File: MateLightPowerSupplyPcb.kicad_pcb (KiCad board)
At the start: 2 copper layers, 59 x 30 mm, 22 parts, among them X1 Power IN, X10 JST ZE 2, X11 JST ZE 2, X12 JST ZE 2, X13 JST ZE 2, X14 JST ZE 2, X15 JST ZE 2, X16 JST ZE 2, X17 JST ZE 2, X18 JST ZE 2, X19 JST ZE 2, X2 Power Out, X20 JST ZE 2, X21 JST ZE 2, X22 JST ZE 2, X3 JST ZE 2, X4 JST ZE 2, X5 JST ZE 2, X6 JST ZE 2, X7 JST ZE 2, X8 JST ZE 2, X9 JST ZE 2

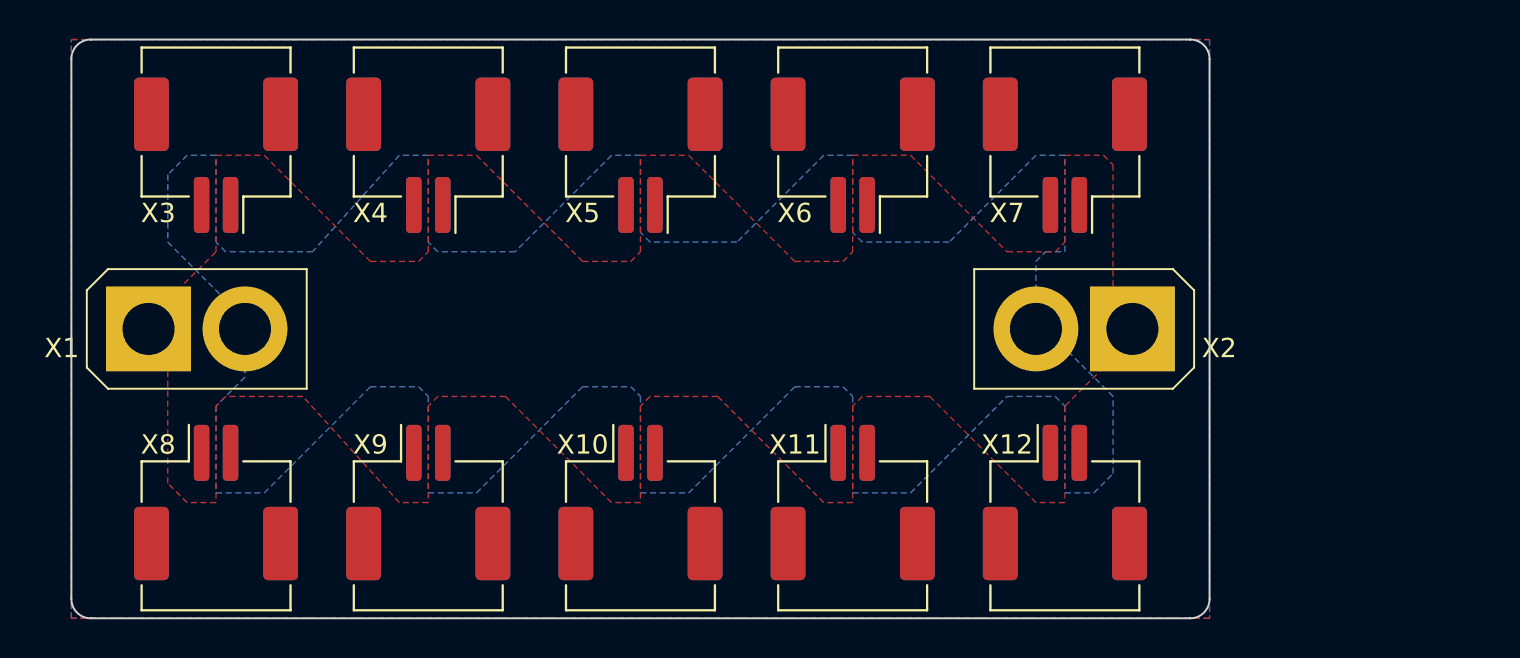
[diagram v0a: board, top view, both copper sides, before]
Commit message: Added mounting options to PCB
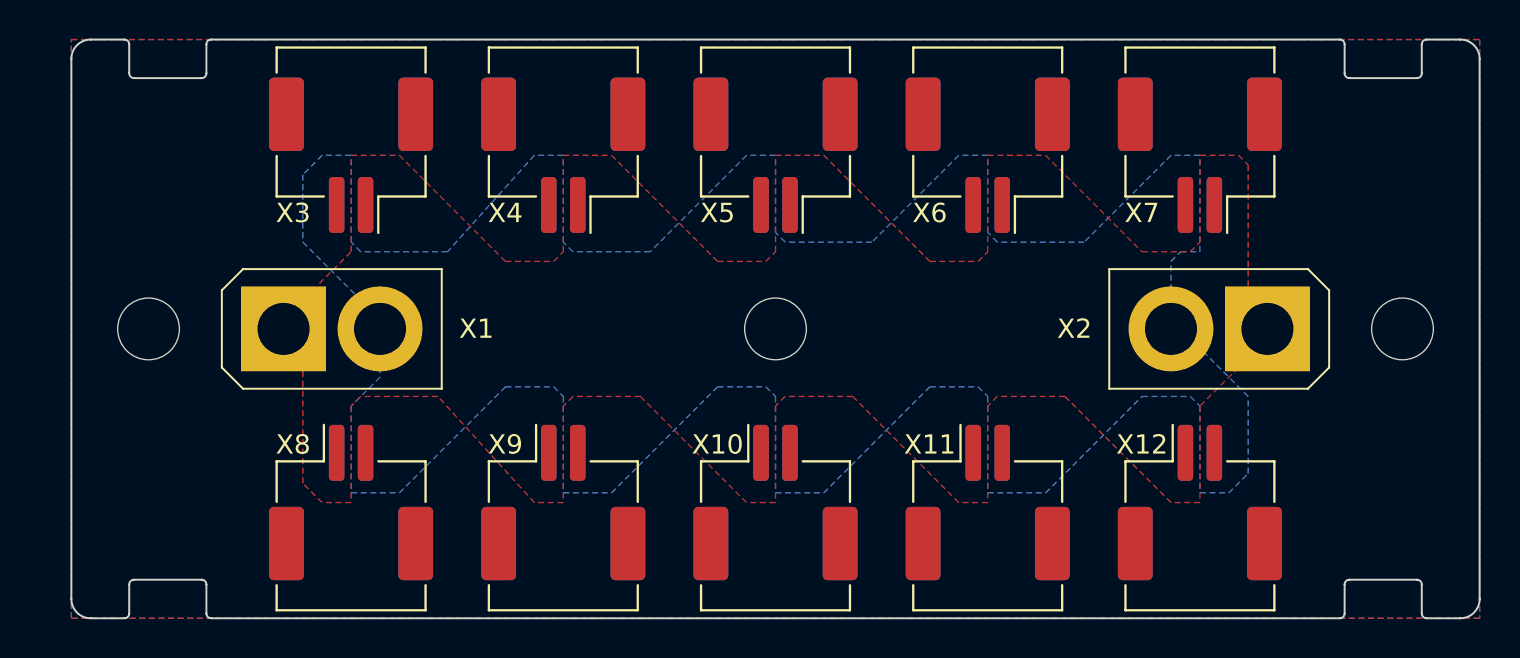
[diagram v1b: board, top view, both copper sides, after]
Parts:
- added H1: MountingHole, MountingHole:MountingHole_3.2mm_M3_DIN965, F.Cu at (104.0, 115.0)
- added H2: MountingHole, MountingHole:MountingHole_3.2mm_M3_DIN965, F.Cu at (136.5, 115.0)
- added H3: MountingHole, MountingHole:MountingHole_3.2mm_M3_DIN965, F.Cu at (169.0, 115.0)
- moved X1 7.00 mm to (113.5, 115.0)
- moved X10 7.00 mm to (136.5, 124.0)
- moved X11 7.00 mm to (147.5, 124.0)
- moved X12 7.00 mm to (158.5, 124.0)
- moved X13 7.00 mm to (114.5, 106.0)
- moved X14 7.00 mm to (125.5, 106.0)
- moved X15 7.00 mm to (136.5, 106.0)
- moved X16 7.00 mm to (147.5, 106.0)
- moved X17 7.00 mm to (158.5, 106.0)
- moved X18 7.00 mm to (114.5, 124.0)
- moved X19 7.00 mm to (125.5, 124.0)
- moved X2 7.00 mm to (159.5, 115.0)
- moved X20 7.00 mm to (136.5, 124.0)
- moved X21 7.00 mm to (147.5, 124.0)
- moved X22 7.00 mm to (158.5, 124.0)
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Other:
- board size 59 x 30 mm -> 73 x 30 mm

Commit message: Changed JST ZE to ZR connectors | added 3D models
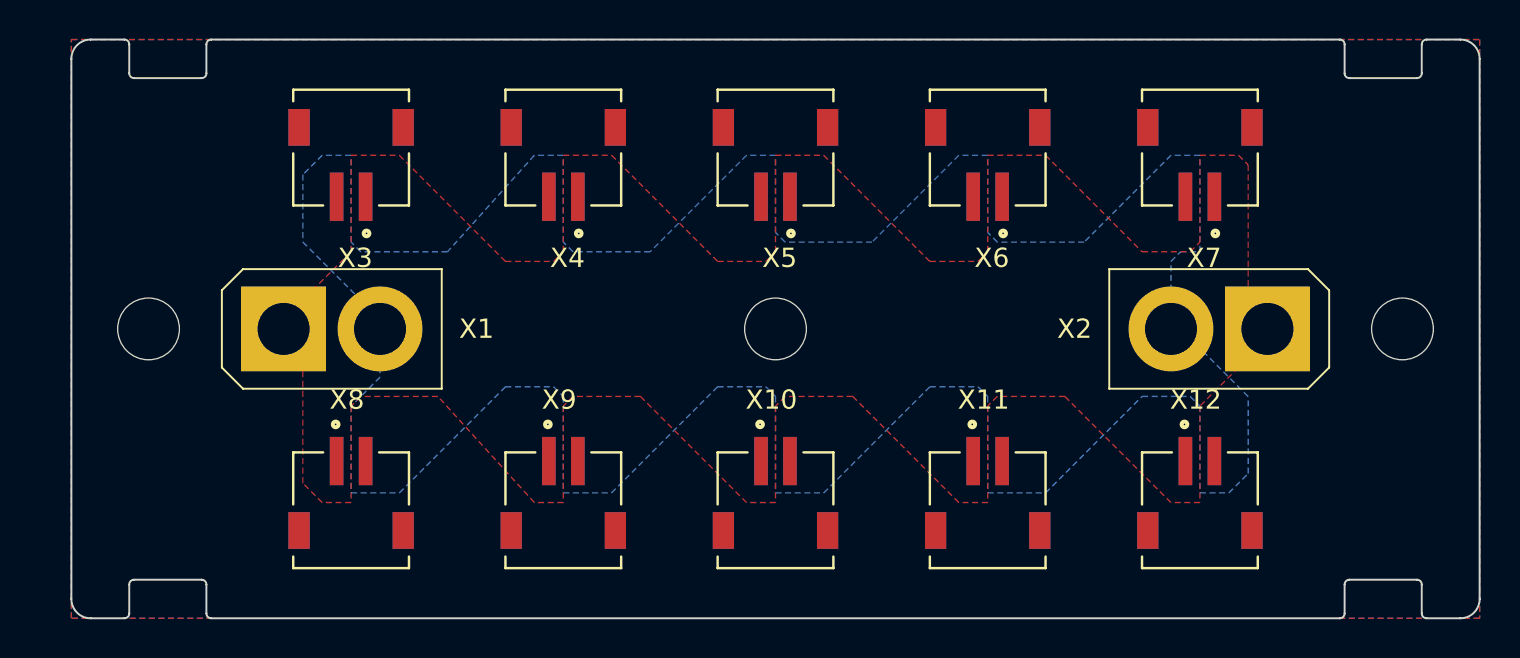
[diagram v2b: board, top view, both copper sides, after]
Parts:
- X10, X11, X12, X13, X14, X15, X16, X17, X18, X19, X20, X21, X22, X3, X4, X5, X6, X7, X8, X9: footprint Connector_JST:JST_ZE_SM02B-ZESS-TB_1x02-1MP_P1.50mm_Horizontal -> h8-Connectors:JST_S2B-ZR-SM4A-TF(LF)(SN)

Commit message: Improvements to fit PCB to ZR/ZH connector
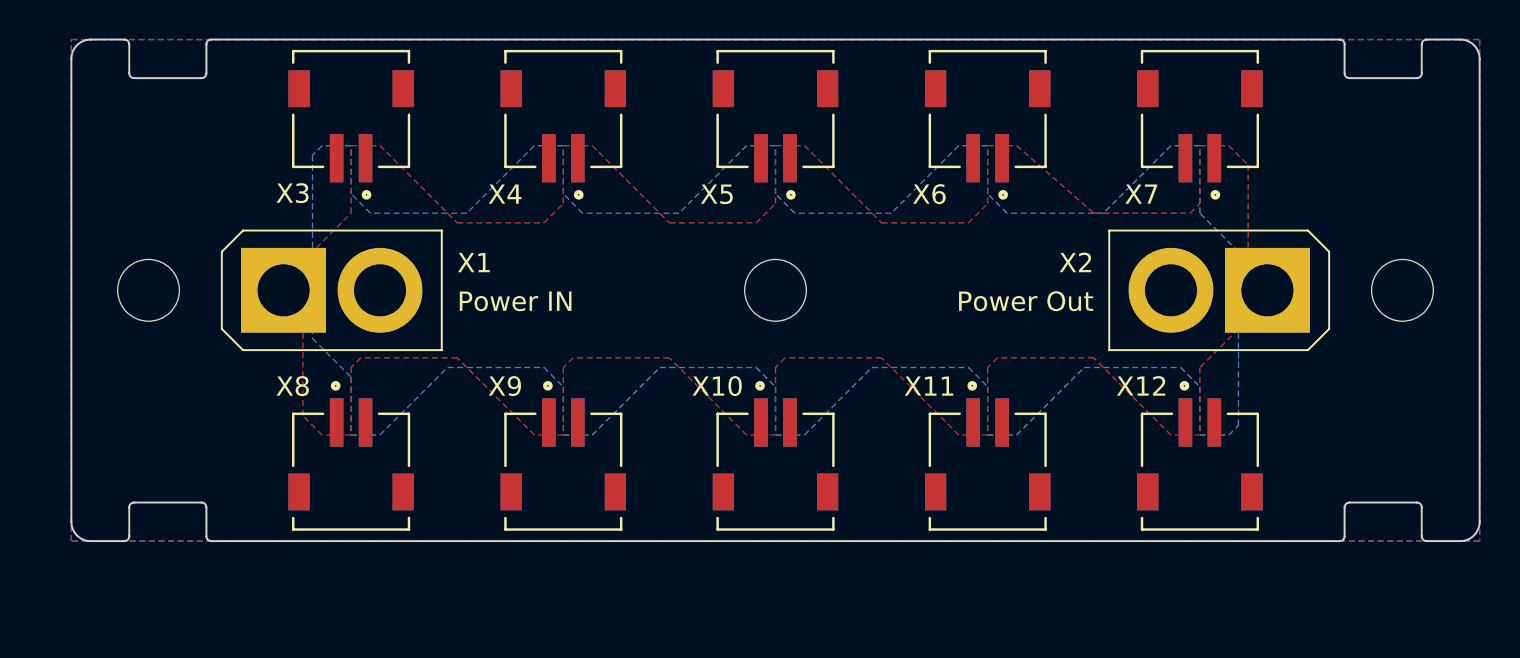
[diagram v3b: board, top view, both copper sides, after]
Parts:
- moved H1 2.00 mm to (104.0, 113.0)
- moved H2 2.00 mm to (136.5, 113.0)
- moved H3 2.00 mm to (169.0, 113.0)
- moved X1 2.00 mm to (113.5, 113.0)
- moved X10 2.00 mm to (136.5, 122.0)
- moved X11 2.00 mm to (147.5, 122.0)
- moved X12 2.00 mm to (158.5, 122.0)
- moved X13 2.00 mm to (158.5, 104.0)
- moved X14 2.00 mm to (147.5, 104.0)
- moved X15 2.00 mm to (136.5, 104.0)
- moved X16 2.00 mm to (125.5, 104.0)
- moved X17 2.00 mm to (114.5, 104.0)
- moved X18 2.00 mm to (158.5, 122.0)
- moved X19 2.00 mm to (147.5, 122.0)
- moved X2 2.00 mm to (159.5, 113.0)
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- renumbered X17 to X13, X16 to X14, X14 to X16, X13 to X17, X22 to X18, X21 to X19, X19 to X21, X18 to X22
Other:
- board size 73 x 30 mm -> 73 x 26 mm

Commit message: Added description and logos to silkscreen
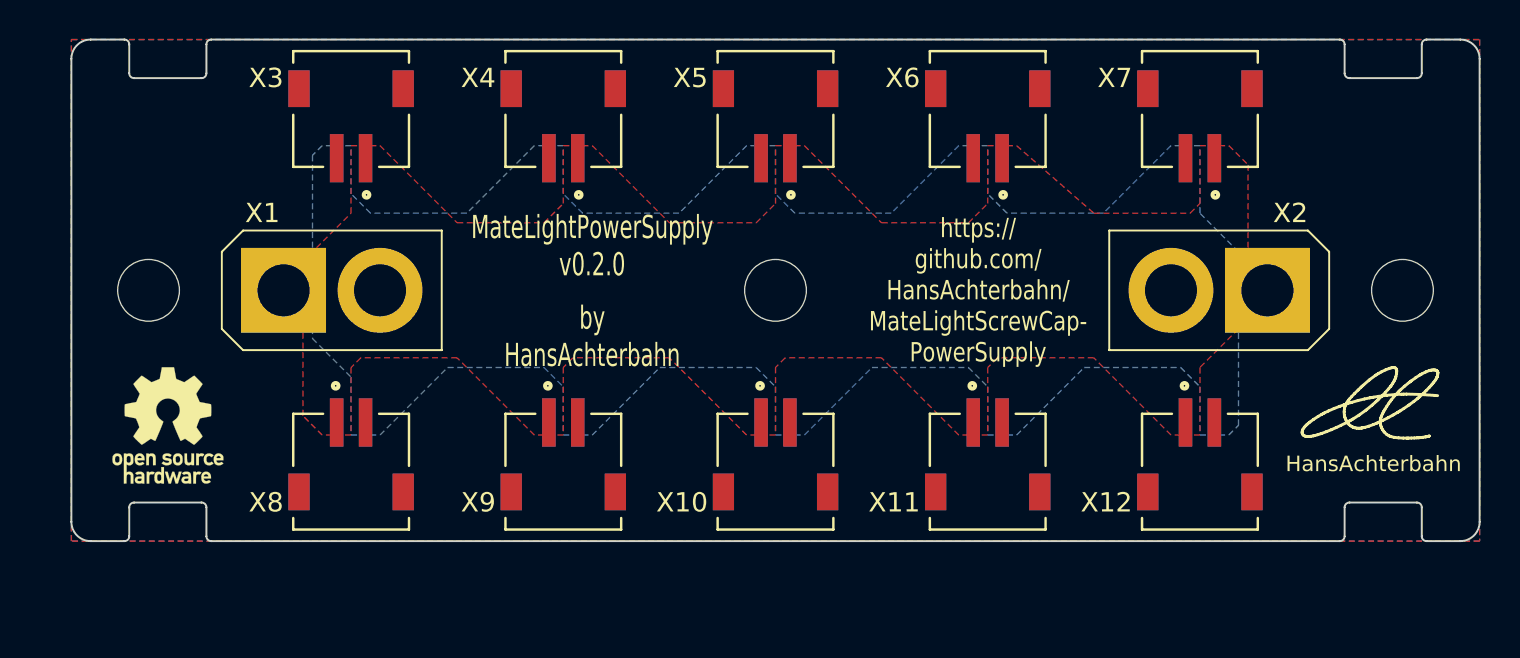
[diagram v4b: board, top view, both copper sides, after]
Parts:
- added REF**: h8-Logo-4mm, h8-Logos:h8-Logo-4mm, F.Cu at (168.0, 119.0)
- added REF**: OSHW-Logo_5.7x6mm_SilkScreen, Symbol:OSHW-Logo_5.7x6mm_SilkScreen, F.Cu at (105.0, 120.0)
- added REF**: KiCad-Logo2_5mm_SilkScreen, Symbol:KiCad-Logo2_5mm_SilkScreen, B.Cu at (147.0, 113.0)
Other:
- board text added: "HansAchterbahn"
- board text added: "MateLightPowerSupply v0.2.0"
- board text added: "by HansAchterbahn"
- board text added: "https:// github.com/ HansAchterbahn/ MateLightScrewCap- PowerSupply"
